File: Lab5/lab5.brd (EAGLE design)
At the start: 100 x 80 mm, 53 parts, among them J1 ISP, U1 ATMEGA128RFA1

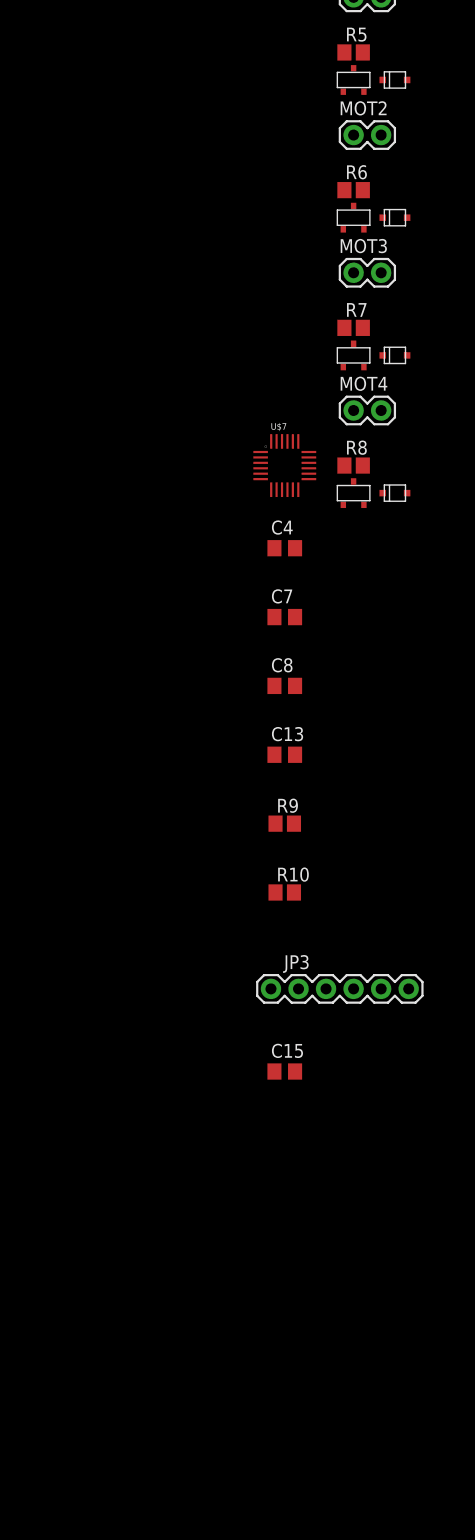
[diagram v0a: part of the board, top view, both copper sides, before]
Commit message: Revamped the lab 5 schematic
Cleaned up the schematic a bunch and condensed the libraries into 1
called lab5_comps.lbr
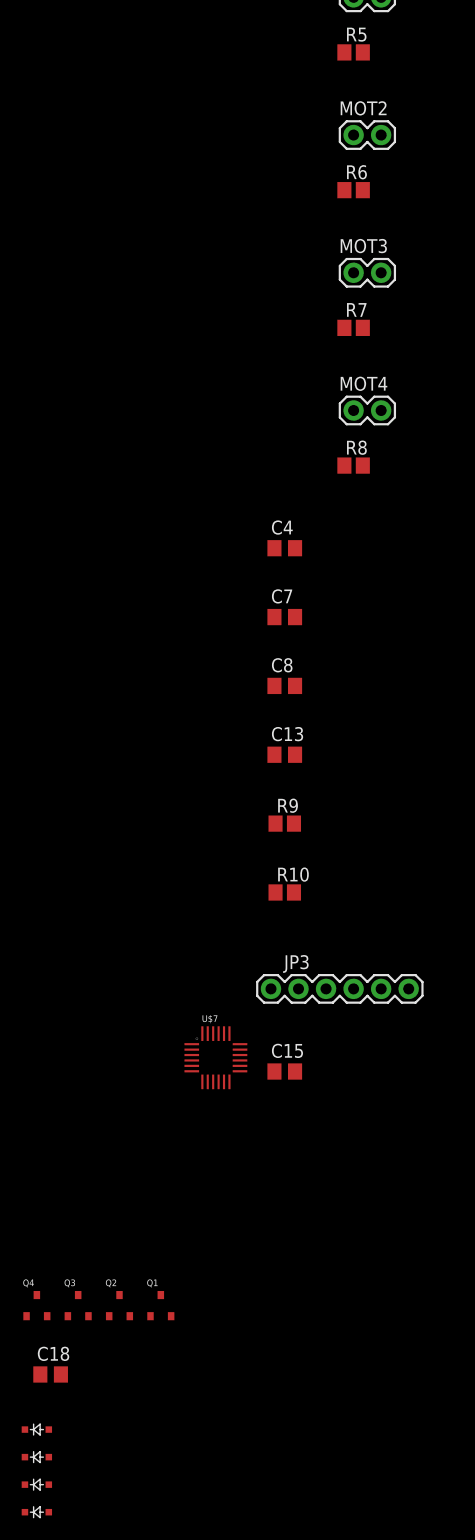
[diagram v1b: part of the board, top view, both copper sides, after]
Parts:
- removed U$3, U$4, U$5, U$6: FET, copter_components:FET
- added C18: 1uF, lab5_comps:C0805
- added Q1, Q2, Q3, Q4: SI2302CDS, lab5_comps:SI2302CDS
- B1: device Lab5:BALUN -> lab5_comps:BALUN
- C1, C10, C11, C13, C14, C15, C2, C3, C4, C5, C6, C7, C8, C9: device Lab5:C0805 -> lab5_comps:C0805
- C12: value 1uF -> 0.01uF; device Lab5:C0805 -> lab5_comps:C0805
- C16, C17: value (none) -> JUMP; device Lab5:C0805 -> lab5_comps:C0805
- D1, D2, D3, D4: value DIODE -> BAS16WS; device copter_components:DIODE -> lab5_comps:BAS16WS
- J1: device Lab5:2X3-NS -> lab5_comps:2X3-NS
- JP1: device Lab5:FTDI_BASIC -> lab5_comps:FTDI_BASIC
- JP2: value (none) -> Battery; device Lab5:1X02 -> lab5_comps:1X02
- JP3: value FTDI -> Serial Debugger; device Lab5:FTDI_BASIC -> lab5_comps:FTDI_BASIC
- LED1, LED2, LED3: device Lab5:CHIP-LED0805 -> lab5_comps:CHIP-LED0805
- MOT1, MOT2, MOT3, MOT4: value (none) -> 20mm; device Lab5:1X02 -> lab5_comps:1X02
- R1, R10, R2, R3, R4, R9: device Lab5:R0805 -> lab5_comps:R0805
- R5, R6, R7, R8: value (none) -> 10k; device Lab5:R0805 -> lab5_comps:R0805
- S1: value (none) -> On/Off; device Lab5:SWITCH-SPDT -> lab5_comps:SWITCH-SPDT
- U$1: device Lab5:ANTENNA-CHIP5 -> lab5_comps:ANTENNA-CHIP5
- U$2: device Lab5:SOT23-DBV -> lab5_comps:SOT23-DBV
- U$7: device lab4_comps:LSM9DS0 -> lab5_comps:LSM9DS0
- U1: device Lab5:QFN-64 -> lab5_comps:QFN-64
- Y1: value (none) -> 16MHz; device Lab5:CRYSTAL-SMD-5X3 -> lab5_comps:CRYSTAL-SMD-5X3
- moved D1 128.8 mm to (-66.0, -307.3)
- moved D2 119.0 mm to (-66.0, -309.9)
- moved D3 109.2 mm to (-66.0, -312.4)
- moved D4 99.6 mm to (-66.0, -315.0)
- moved U$7 55.0 mm to (-49.5, -273.1)
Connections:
- net N$13 renamed RFN
- net N$14 renamed RFP
- removed net SCH: J1.3
- net 3V: now also C18.1, D1.P$1, D2.P$1, D3.P$1, D4.P$1, U$7.15, U$7.16, U$7.17, U$7.18; no longer D1.P$NEG, D2.P$NEG, D3.P$NEG, D4.P$NEG, U$7.P$15, U$7.P$16, U$7.P$17, U$7.P$18
- net GND: now also C18.2, Q1.S, Q2.S, Q3.S, Q4.S, U$7.2, U$7.22, U$7.23, U$7.3, U$7.4, U$7.5, U$7.6; no longer U$3.P$2, U$4.P$2, U$5.P$2, U$6.P$2, U$7.P$2, U$7.P$22, U$7.P$23, U$7.P$3, U$7.P$4, U$7.P$5, U$7.P$6
- net N$18: now also D1.P$2, Q1.D; no longer D1.P$POS, U$3.P$3
- net N$20: now also D2.P$2, Q2.D; no longer D2.P$POS, U$4.P$3
- net N$22: now also D3.P$2, Q3.D; no longer D3.P$POS, U$5.P$3
- net N$24: now also D4.P$2, Q4.D; no longer D4.P$POS, U$6.P$3
- net N$25: now also U$7.8; no longer U$7.P$8
- net N$26: now also U$7.9; no longer U$7.P$9
- net N$27: now also U$7.7; no longer U$7.P$7
- net N$29: now also U$7.19; no longer U$7.P$19
- net N$30: now also U$7.20; no longer U$7.P$20
- net PB5: now also Q1.G; no longer U$3.P$1
- net PE3: now also Q3.G; no longer U$5.P$1
- net PE4: now also Q4.G; no longer U$6.P$1
- net PE5: now also Q2.G; no longer U$4.P$1
- net SCK: now also J1.3
- net SCL: now also U$7.21; no longer U$7.P$21
- net SDA: now also U$7.24; no longer U$7.P$24

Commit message: Corrected Schematic and some of the board
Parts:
- C16, C17: device lab5_comps:C0805 -> lab5_comps:R0805
- moved D1 336.1 mm to (-2.24, 22.7)
- moved Q1 327.8 mm to (-0.31, 27.4)
- moved D2 321.4 mm to (19.9, -0.18)
- moved C18 319.4 mm to (-3.07, 11.1)
- moved D4 313.6 mm to (-26.8, -3.86)
- moved Q2 307.2 mm to (25.0, -0.28), turned to 270 degrees
- moved Q4 299.2 mm to (-27.0, 0.76), turned to 90 degrees
- moved D3 296.8 mm to (7.96, -25.0)
- moved Q3 276.4 mm to (-0.37, -26.5), turned to 180 degrees
- moved C15 264.9 mm to (24.9, -18.3)
- moved U$7 263.5 mm to (-5.33, -13.2)
- moved JP3 251.9 mm to (18.1, -22.7)
- moved R10 247.1 mm to (1.92, -14.8)
- moved R9 244.2 mm to (1.92, -11.5)
- moved C13 228.3 mm to (-11.1, -19.1)
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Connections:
- removed net N$1: C14.2, S1.1, U$2.1, U$2.3
- new net VBAT: C14.2, D1.P$1, D2.P$1, D3.P$1, D4.P$1, MOT1.2, MOT2.2, MOT3.2, MOT4.2, S1.1, U$2.1, U$2.3
- net 3V: no longer D1.P$1, D2.P$1, D3.P$1, D4.P$1, MOT1.2, MOT2.2, MOT3.2, MOT4.2
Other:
- board size 100 x 80 mm -> 130 x 130 mm
